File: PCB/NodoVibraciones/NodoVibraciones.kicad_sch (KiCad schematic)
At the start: 17 parts, among them J1 batería, J2 UART, J3 MPU6050, SW1 SW_Push, SW2 SW_Push, SW3 SW_Nidec_CAS-120A1, U1 ESP-07, U2 MPU-6050

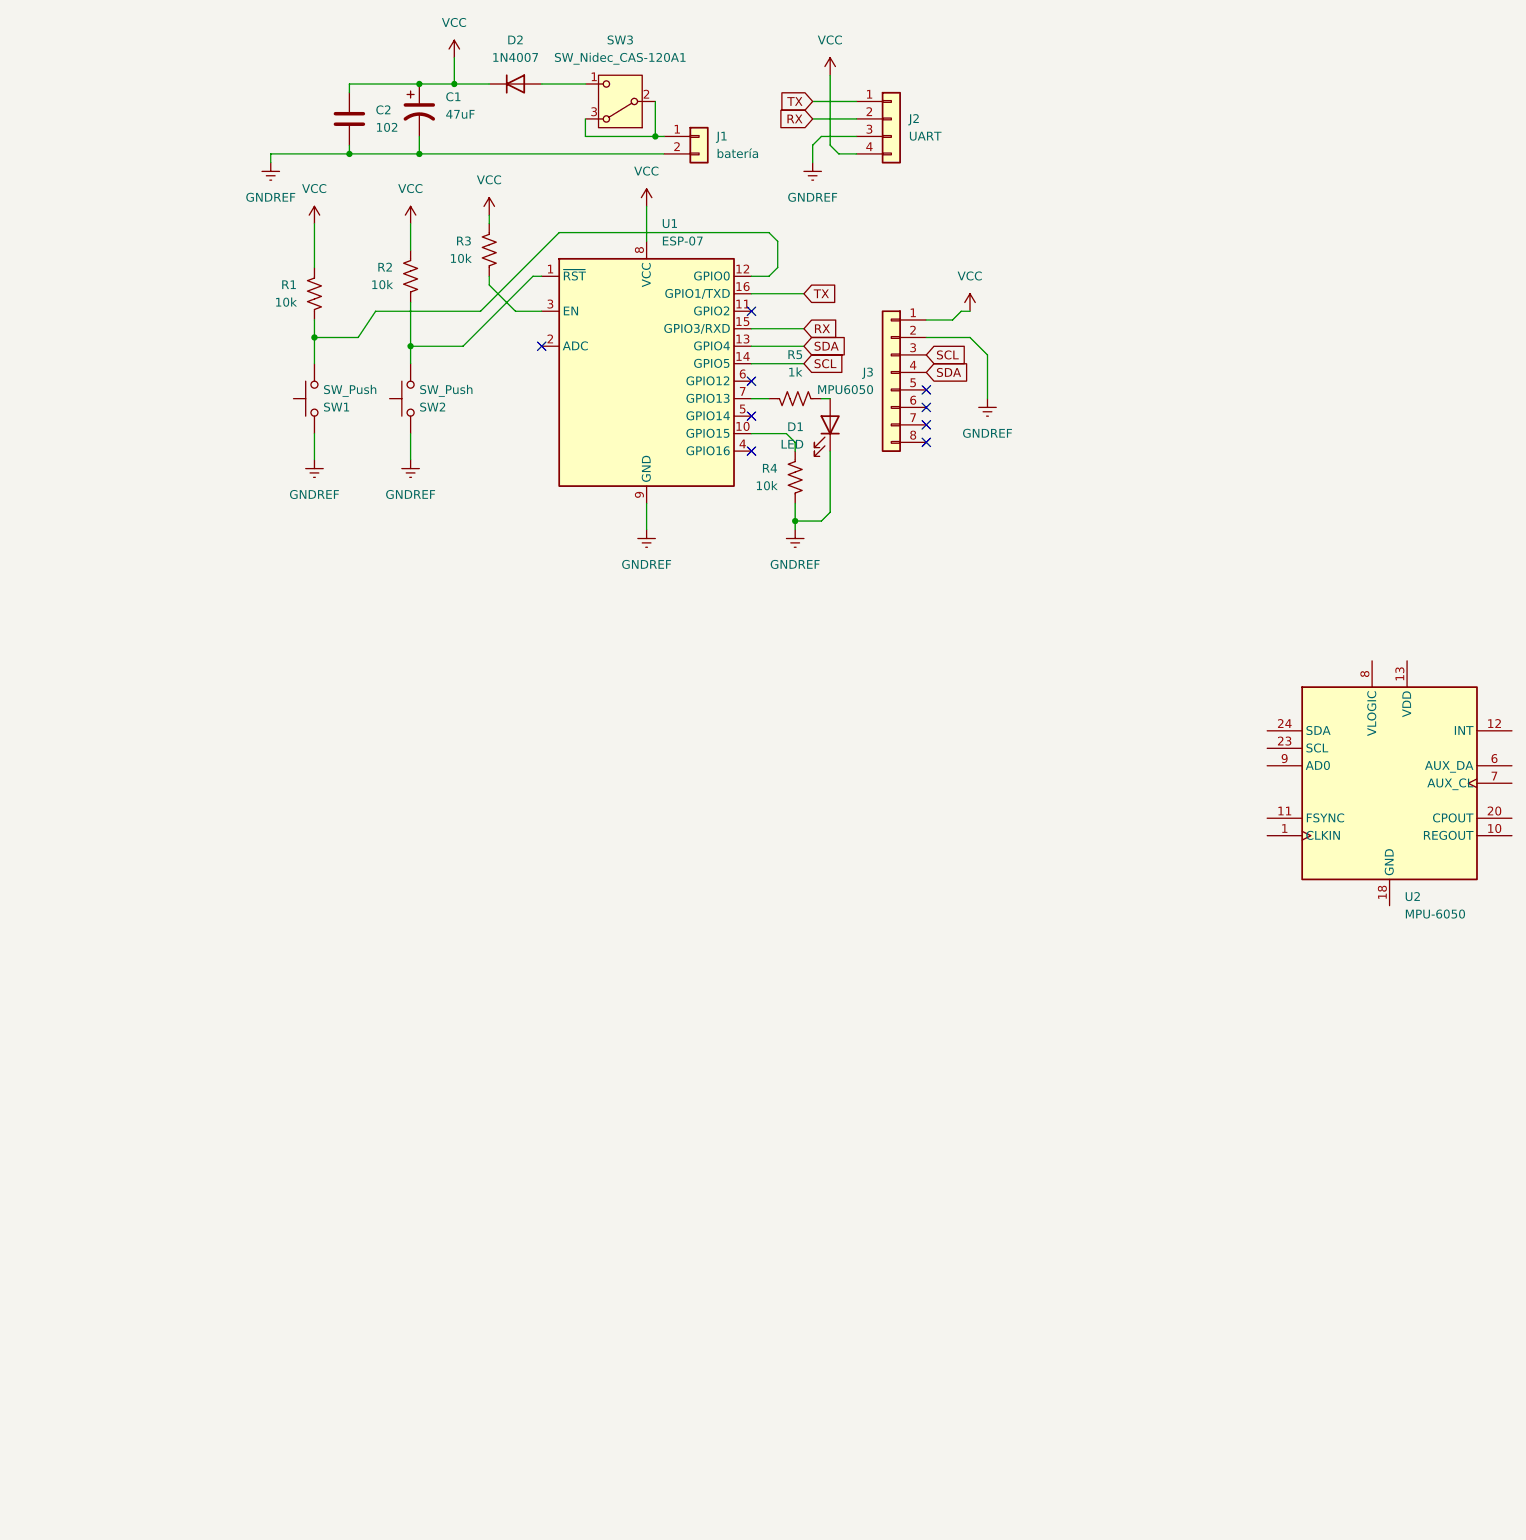
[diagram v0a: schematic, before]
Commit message: Se creó PCB v0.0.1 de nodo VibraNet
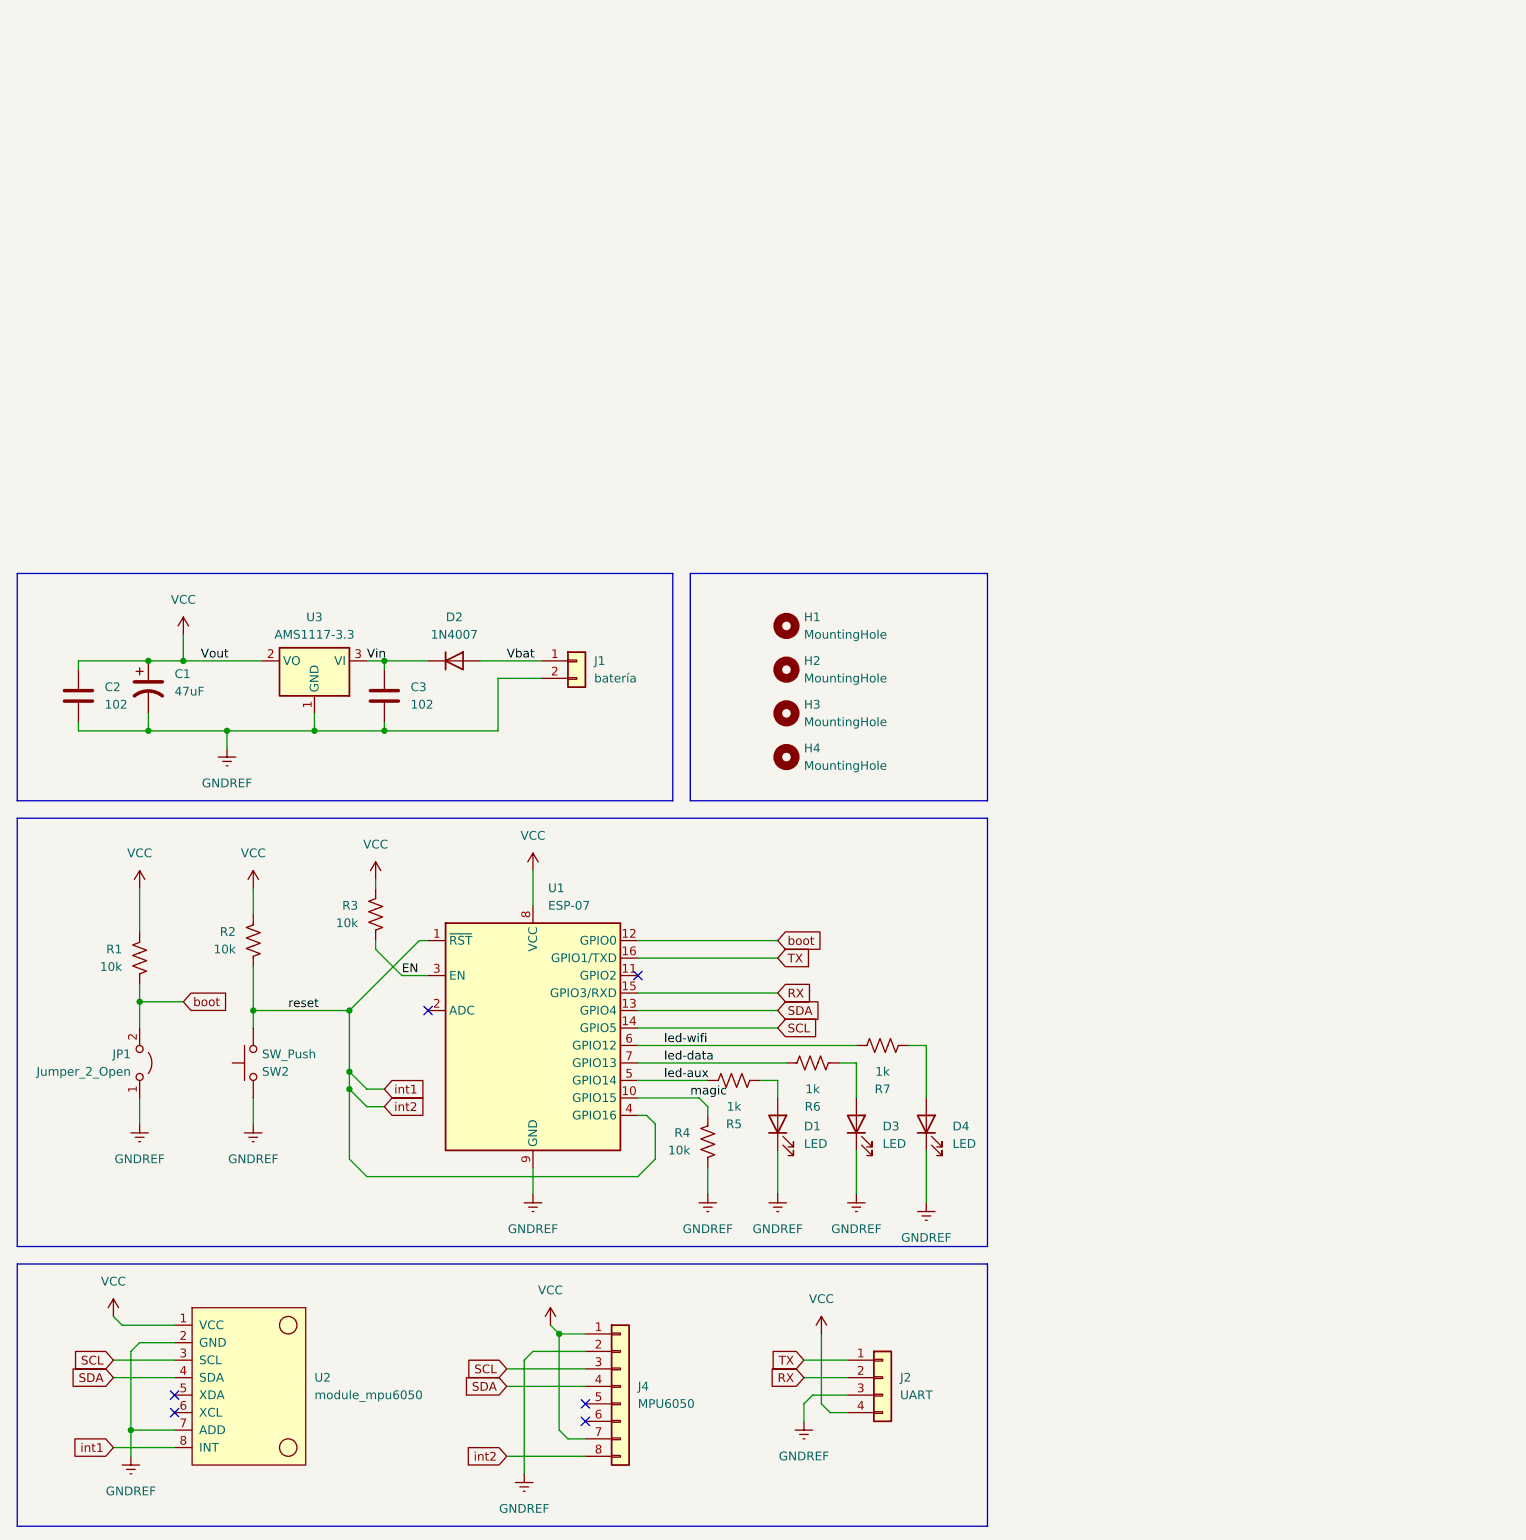
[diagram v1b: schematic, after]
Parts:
- removed J3: MPU6050, Connector_PinSocket_2.54mm:PinSocket_1x08_P2.54mm_Vertical, symbol Connector_Generic:Conn_01x08
- removed SW1: SW_Push, Button_Switch_SMD:SW_SPST_PTS645, symbol Switch:SW_Push
- removed SW3: SW_Nidec_CAS-120A1, Button_Switch_THT:SW_Slide_SPDT_Angled_CK_OS102011MA1Q, symbol Switch:SW_Nidec_CAS-120A1
- removed U2: MPU-6050, Sensor_Motion:InvenSense_QFN-24_4x4mm_P0.5mm, symbol Sensor_Motion:MPU-6050
- added C3: 102, Capacitor_THT:C_Disc_D5.0mm_W2.5mm_P2.50mm, symbol Device:C
- added D3, D4: LED, LED_THT:LED_D5.0mm, symbol Device:LED
- added H1, H2, H3, H4: MountingHole, MountingHole:MountingHole_3.2mm_M3, symbol Mechanical:MountingHole
- added J4: MPU6050, Connector_PinSocket_2.54mm:PinSocket_1x08_P2.54mm_Vertical, symbol Connector_Generic:Conn_01x08
- added JP1: Jumper_2_Open, Jumper:SolderJumper-2_P1.3mm_Open_RoundedPad1.0x1.5mm, symbol Jumper:Jumper_2_Open
- added R6, R7: 1k, Resistor_THT:R_Axial_DIN0207_L6.3mm_D2.5mm_P10.16mm_Horizontal, symbol Device:R_US
- added U2: module_mpu6050, USINI_sensors:module_mpu6050, symbol USINI_sensors:module_mpu6050
- added U3: AMS1117-3.3, Package_TO_SOT_SMD:SOT-223-3_TabPin2, symbol Regulator_Linear:AMS1117-3.3
- C1: footprint Capacitor_SMD:CP_Elec_5x5.4 -> Capacitor_THT:CP_Radial_D5.0mm_P2.50mm
- C2: footprint Capacitor_SMD:C_1206_3216Metric_Pad1.33x1.80mm_HandSolder -> Capacitor_THT:C_Disc_D5.0mm_W2.5mm_P2.50mm
- D1: footprint LED_SMD:LED_1206_3216Metric_Pad1.42x1.75mm_HandSolder -> LED_THT:LED_D5.0mm
- D2: footprint Diode_SMD:D_SMA_Handsoldering -> Diode_THT:D_A-405_P10.16mm_Horizontal
- R1, R2, R3, R4, R5: footprint Resistor_SMD:R_1206_3216Metric_Pad1.30x1.75mm_HandSolder -> Resistor_THT:R_Axial_DIN0207_L6.3mm_D2.5mm_P10.16mm_Horizontal
- SW2: footprint Button_Switch_SMD:SW_SPST_PTS645 -> Button_Switch_THT:SW_PUSH_6mm_H4.3mm
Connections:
- net GNDREF: now also C3.2, D3.1 (K), D4.1 (K), J4.2 (Pin_2), JP1.1 (A), U2.2 (GND), U2.7 (ADD), U3.1 (GND)
- net SCL: now also J4.3 (Pin_3), U2.3 (SCL)
- net SDA: now also J4.4 (Pin_4), U2.4 (SDA)
- net VCC: now also J4.1 (Pin_1), J4.7 (Pin_7), U2.1 (VCC), U3.2 (VO); no longer D2.1 (K)
- net int1: now reaches R2.1, SW2.1, U1.1 (~{RST})
- net int1: now also U1.4 (GPIO16), J4.8 (Pin_8), U2.8 (INT)
- net magic: now reaches R4.2, U1.10 (GPIO15)
- net boot: now reaches R1.1, U1.12 (GPIO0)
- net boot: now also JP1.2 (B)
- net EN: now reaches R3.1, U1.3 (EN)
- net led-aux: now reaches U1.5 (GPIO14)
- net led-aux: now also R5.2
- net led-wifi: now reaches U1.6 (GPIO12)
- net led-wifi: now also R7.2
- net led-data: now reaches U1.7 (GPIO13)
- net led-data: now also R6.2; no longer R5.2
- net Vbat: now reaches D2.2 (A)
- net Vbat: now also J1.1 (Pin_1)
- new net: D4.2 (A), R7.1
- new net: D3.2 (A), R6.1
- new net Vin: C3.1, D2.1 (K), U3.3 (VI)
- no-connect marks 9 -> 6
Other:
- company: (none) -> UNIVERSIDAD NACIONAL DE CUYO - FACULTAD DE INGENIERIA
- title: (none) -> VibraNet (Red de nodos sismoreceptores)
- moved on the sheet: C1, C2, D1, D2, J1, J2, R1, R2, R3, R4, R5, SW2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

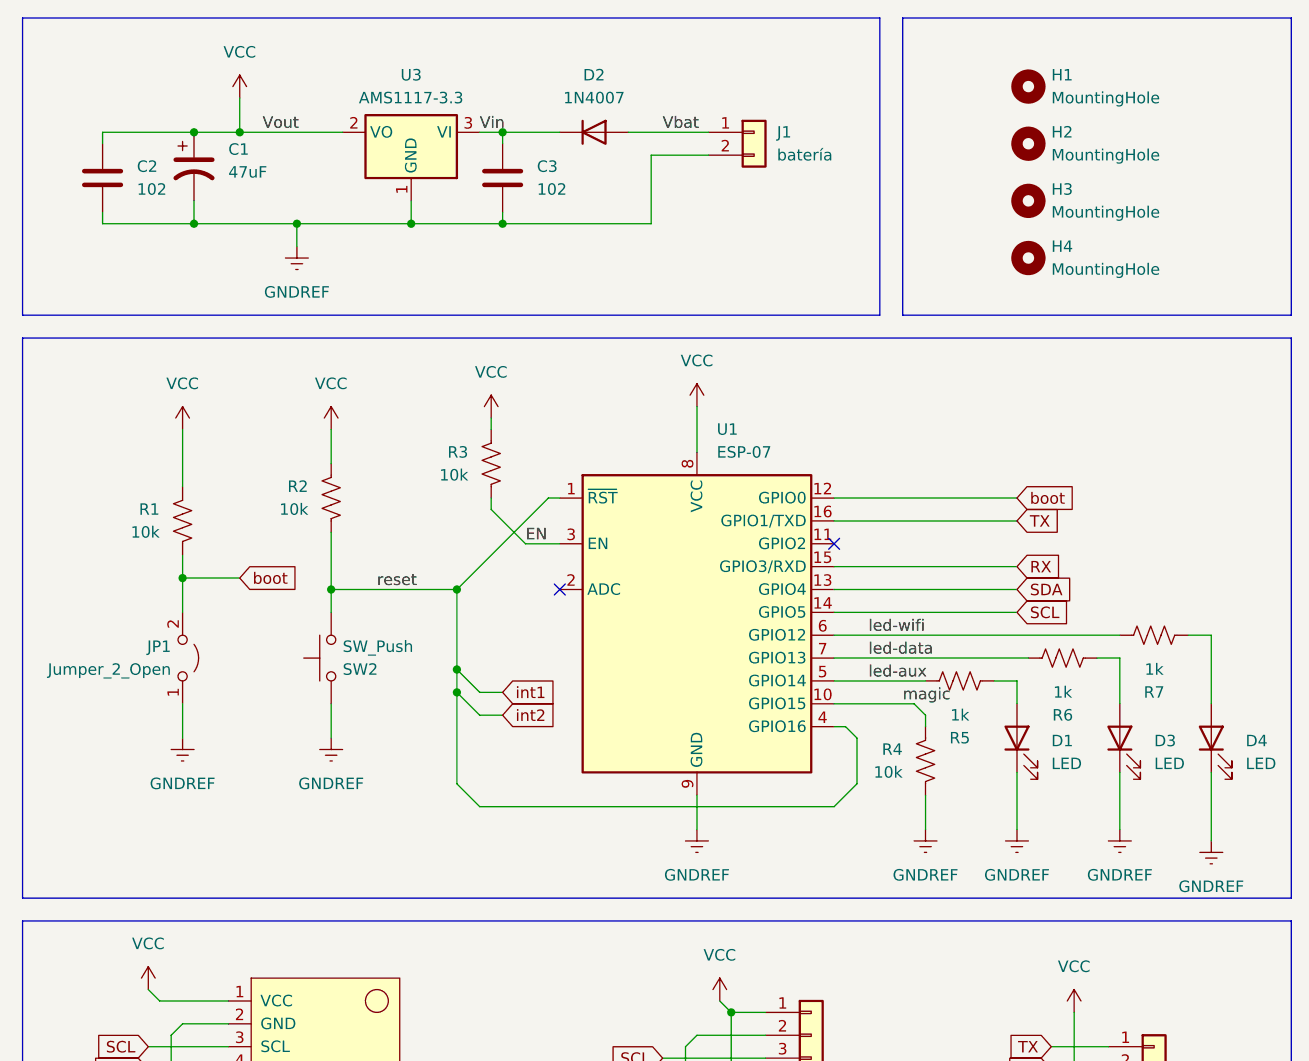
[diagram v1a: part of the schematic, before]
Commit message: Se implementaron interrupciones y diseño de PCB v1.0.8
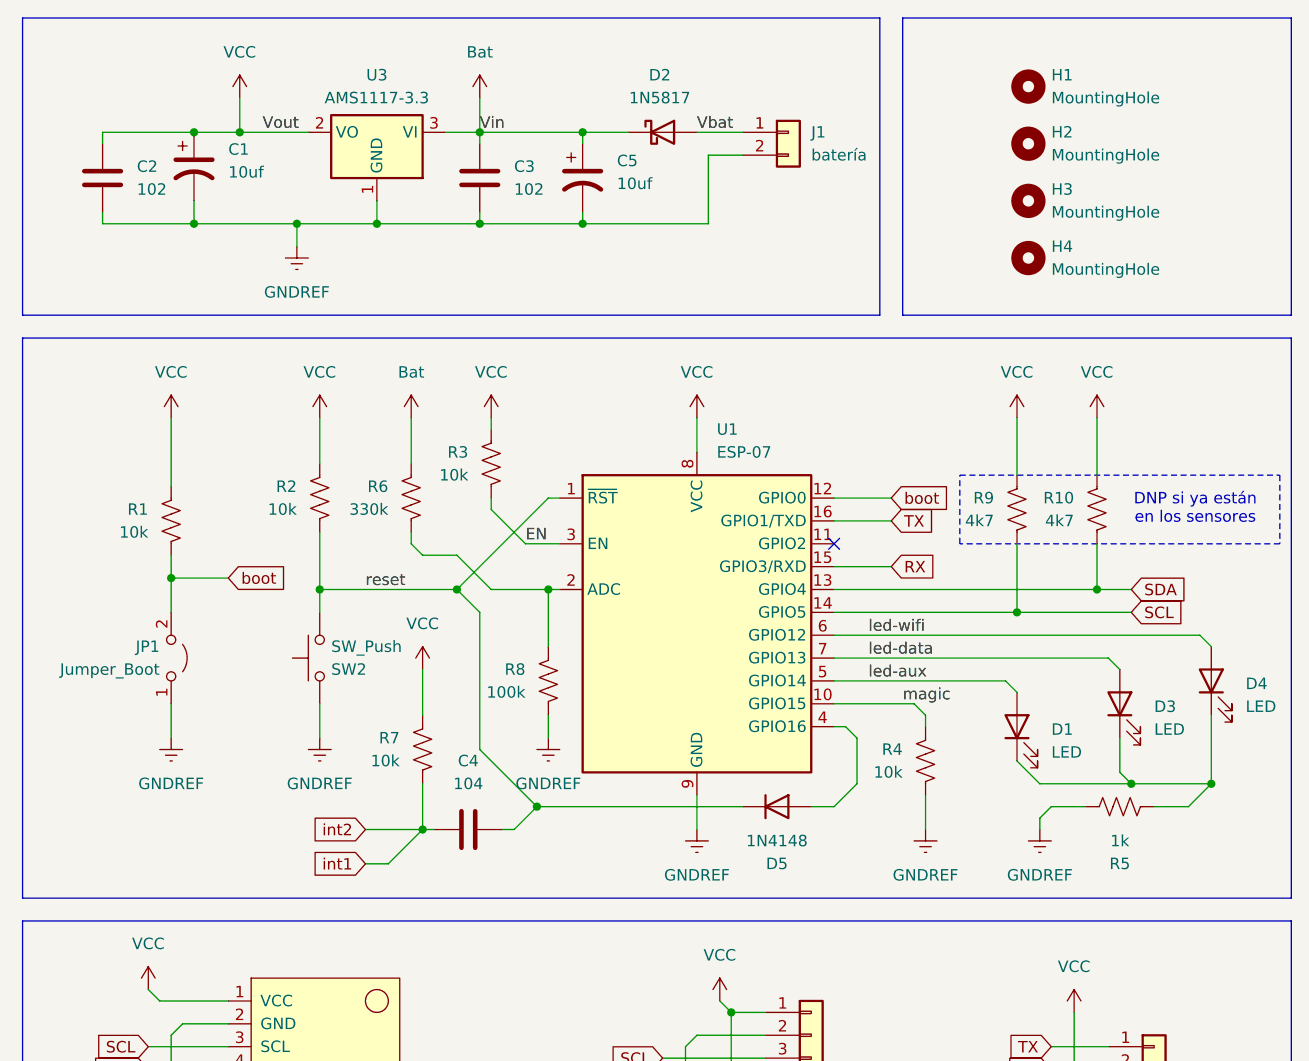
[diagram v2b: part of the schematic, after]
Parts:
- removed D2: 1N4007, Diode_THT:D_A-405_P10.16mm_Horizontal, symbol Diode:1N4007
- added C4: 104, Capacitor_THT:C_Disc_D5.0mm_W2.5mm_P2.50mm, symbol Device:C
- added C5: 10uf, Capacitor_THT:CP_Radial_D5.0mm_P2.50mm, symbol Device:C_Polarized_US
- added D2: 1N5817, Diode_THT:D_DO-41_SOD81_P10.16mm_Horizontal, symbol Diode:1N5817
- added D5: 1N4148, Diode_THT:D_DO-35_SOD27_P7.62mm_Horizontal, symbol Diode:1N4148
- added R10, R9: 4k7, Resistor_THT:R_Axial_DIN0207_L6.3mm_D2.5mm_P10.16mm_Horizontal, symbol Device:R_US
- added R8: 100k, Resistor_THT:R_Axial_DIN0207_L6.3mm_D2.5mm_P10.16mm_Horizontal, symbol Device:R_US
- C1: value 47uF -> 10uf
- JP1: value Jumper_2_Open -> Jumper_Boot
- R6: value 1k -> 330k
- R7: value 1k -> 10k
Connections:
- net GNDREF: now also R5.2, C5.2, R8.1; no longer D1.1 (K), D3.1 (K), D4.1 (K)
- net SCL: now also R9.1
- net SDA: now also R10.1
- net VCC: now also R7.2, R10.2, R9.2
- net Vbat: now also D2.2 (A)
- net int1: now also R7.1, C4.2; no longer R2.1, SW2.1, U1.1 (~{RST}), U1.4 (GPIO16)
- net led-aux: now also D1.2 (A); no longer R5.2
- net led-data: now also D3.2 (A); no longer R6.2
- net led-wifi: now also D4.2 (A); no longer R7.2
- net at R5.1: now also D1.1 (K), D3.1 (K), D4.1 (K); no longer D1.2 (A)
- net at U1.2 (ADC): now also R6.1, R8.2
- net Vin renamed Bat
- net Bat: now also R6.2, C5.1, D2.1 (K)
- new net: D5.2 (A), U1.4 (GPIO16)
- new net reset: C4.1, D5.1 (K), R2.1, SW2.1, U1.1 (~{RST})
- no-connect marks 6 -> 5
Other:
- note added: "DNP si ya están en los sensores"
- moved on the sheet: C3, D1, D3, D4, J1, JP1, R1, R2, R5, SW2, U3

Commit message: Lanzamiento primer prototipo funcional ESP07 verHW1.5
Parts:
- removed C4: 104, Capacitor_THT:C_Disc_D5.0mm_W2.5mm_P2.50mm, symbol Device:C
- removed H4: MountingHole, MountingHole:MountingHole_3.2mm_M3, symbol Mechanical:MountingHole
- added C4: 10uF, Capacitor_THT:CP_Radial_D5.0mm_P2.50mm, symbol Device:C_Polarized_US
- added R11: 10k, Resistor_THT:R_Axial_DIN0207_L6.3mm_D2.5mm_P7.62mm_Horizontal, symbol Device:R_US
- C1, C5: value 10uf -> 100uf
- C2, C3: value 102 -> 104
- R1, R10, R2, R5, R6, R7, R8, R9: footprint Resistor_THT:R_Axial_DIN0207_L6.3mm_D2.5mm_P10.16mm_Horizontal -> Resistor_THT:R_Axial_DIN0207_L6.3mm_D2.5mm_P7.62mm_Horizontal
- R4: value 10k -> 4k7; footprint Resistor_THT:R_Axial_DIN0207_L6.3mm_D2.5mm_P10.16mm_Horizontal -> Resistor_THT:R_Axial_DIN0207_L6.3mm_D2.5mm_P7.62mm_Horizontal
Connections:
- net VCC: now also R11.2
- net int1: now also C4.2
- net reset: now also D5.2 (A), C4.1; no longer D5.1 (K)
- net at U1.11 (GPIO2): now also R11.1
- net at U1.4 (GPIO16): now also D5.1 (K); no longer D5.2 (A)
- no-connect marks 5 -> 4
